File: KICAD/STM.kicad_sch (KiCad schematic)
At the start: 1 part, among them IC5 STM32F746BGT6

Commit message: BT + PCM1808
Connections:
- net SAI1_MCLK_A/SCKI: now reaches IC5.1 (PE2)
- net USART_TX: now reaches IC5.143 (PA9)
- net USART_RX: now reaches IC5.144 (PA10)
- net SAI1_FS_A/LRCK: now reaches IC5.3 (PE4)
- net SAI1_SCK_A/BCK: now reaches IC5.4 (PE5)
- net JACK_DET: now reaches IC5.45 (PA2)
- net SAI1_SD_A/DOUT: now reaches IC5.5 (PE6)
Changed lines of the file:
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@@
 	(generator_version "9.0")
 	(paper "A3")
+	(wire
+		(pts
+			(xy 120.65 81.28) (xy 135.89 81.28)
+		)
+		(stroke
+			(width 0)
+			(type default)
+		)
+	)
+	(wire
+		(pts
+			(xy 280.67 101.6) (xy 292.1 101.6)
+		)
+		(stroke
+			(width 0)
+			(type default)
+		)
+	)
+	(wire
+		(pts
+			(xy 280.67 104.14) (xy 292.1 104.14)
+		)
+		(stroke
+			(width 0)
+			(type default)
+		)
+	)
+	(wire
+		(pts
+			(xy 120.65 78.74) (xy 135.89 78.74)
+		)
+		(stroke
+			(width 0)
+			(type default)
+		)
+	)
+	(wire
+		(pts
+			(xy 120.65 71.12) (xy 135.89 71.12)
+		)
+		(stroke
+			(width 0)
+			(type default)
+		)
+	)
+	(wire
+		(pts
+			(xy 120.65 76.2) (xy 135.89 76.2)
+		)
+		(stroke
+			(width 0)
+			(type default)
+		)
+	)
+	(hierarchical_label "USART_TX"
+		(shape input)
+		(at 292.1 104.14 0)
+		(effects
+			(font
+				(size 1.27 1.27)
+			)
+			(justify left)
+		)
+	)
+	(hierarchical_label "SAI1_FS_A{slash}LRCK"
+		(shape input)
+		(at 120.65 76.2 180)
+		(effects
+			(font
+				(size 1.27 1.27)
+			)
+			(justify right)
+		)
+	)
+	(hierarchical_label "SAI1_SCK_A{slash}BCK"
+		(shape input)
+		(at 120.65 78.74 180)
+		(effects
+			(font
+				(size 1.27 1.27)
+			)
+			(justify right)
+		)
+	)
+	(hierarchical_label "SAI1_MCLK_A{slash}SCKI"
+		(shape input)
+		(at 120.65 71.12 180)
+		(effects
+			(font
+				(size 1.27 1.27)
+			)
+			(justify right)
+		)
+	)
+	(hierarchical_label "USART_RX"
+		(shape input)
+		(at 292.1 101.6 0)
+		(effects
+			(font
+				(size 1.27 1.27)
+			)
+			(justify left)
+		)
+	)
+	(hierarchical_label "SAI1_SD_A{slash}DOUT"
+		(shape input)
+		(at 120.65 81.28 180)
+		(effects
+			(font
+				(size 1.27 1.27)
+			)
+			(justify right)
+		)
+	)
+	(hierarchical_label "JACK_DET"
+		(shape input)
+		(at 135.89 182.88 180)
+		(effects
+			(font
+				(size 1.27 1.27)
+			)
+			(justify right)
+		)
+	)
 	(symbol
 		(lib_id "STM32F746BGT6:STM32F746BGT6")

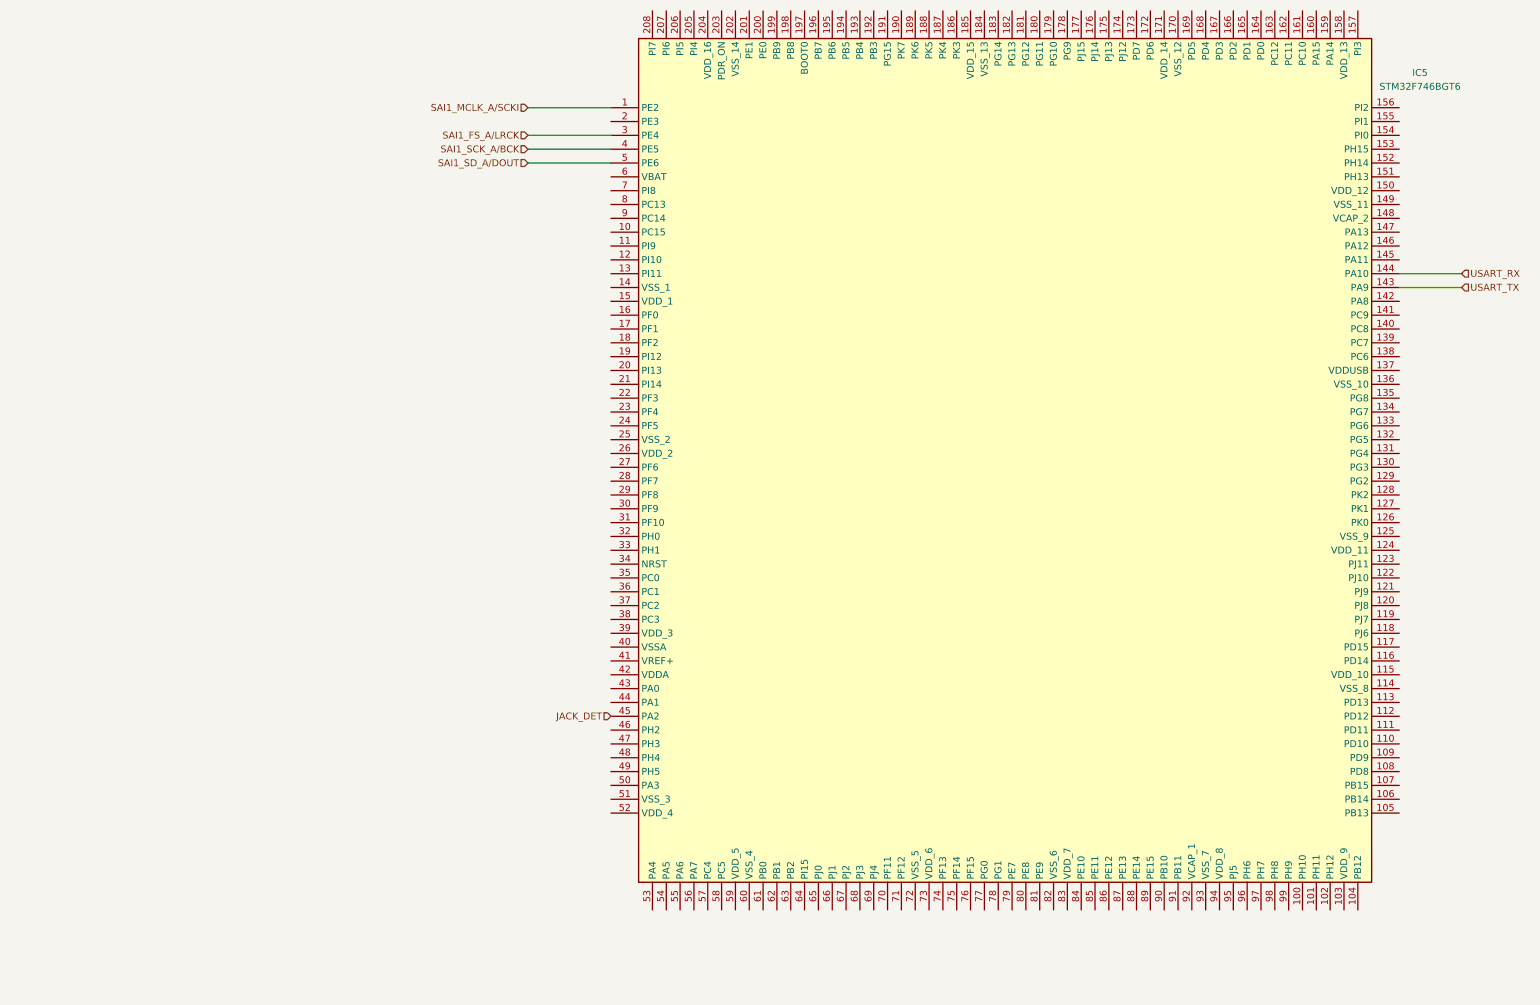
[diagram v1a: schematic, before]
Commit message: Config ports DAC + Ampli
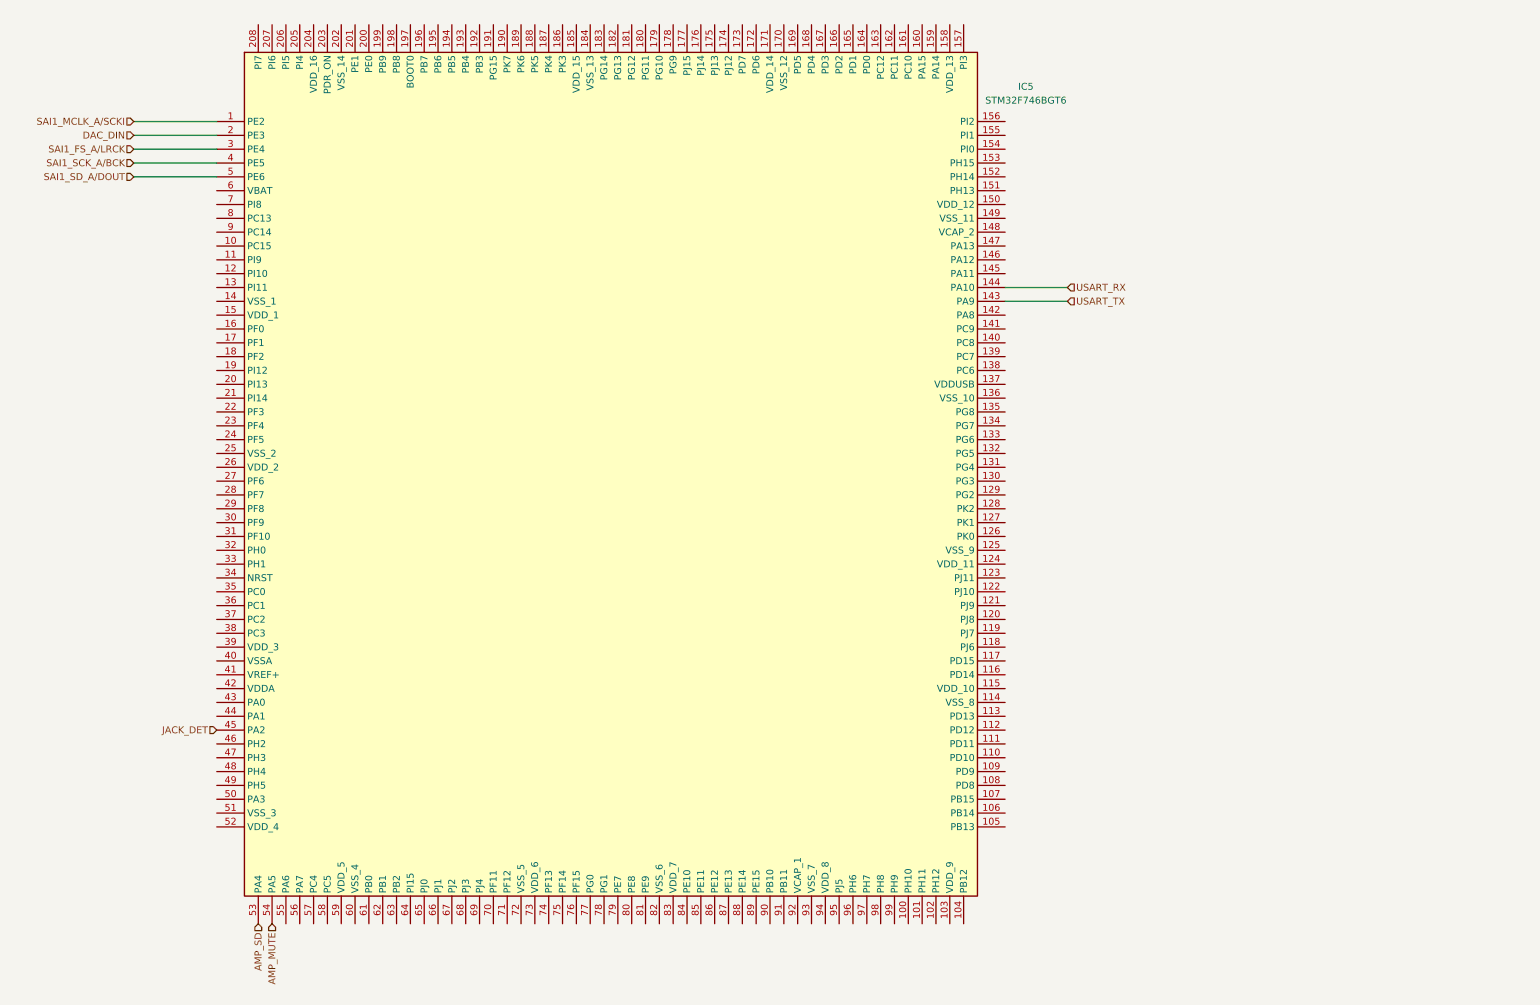
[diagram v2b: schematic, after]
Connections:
- net DAC_DIN: now reaches IC5.2 (PE3)
- net AMP_SD: now reaches IC5.53 (PA4)
- net AMP_MUTE: now reaches IC5.54 (PA5)
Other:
- moved on the sheet: IC5
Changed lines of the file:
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@@
 	(wire
 		(pts
-			(xy 120.65 81.28) (xy 135.89 81.28)
-		)
-		(stroke
-			(width 0)
-			(type default)
-		)
-	)
-	(wire
-		(pts
-			(xy 280.67 101.6) (xy 292.1 101.6)
-		)
-		(stroke
-			(width 0)
-			(type default)
-		)
-	)
-	(wire
-		(pts
-			(xy 280.67 104.14) (xy 292.1 104.14)
-		)
-		(stroke
-			(width 0)
-			(type default)
-		)
-	)
-	(wire
-		(pts
-			(xy 120.65 78.74) (xy 135.89 78.74)
-		)
-		(stroke
-			(width 0)
-			(type default)
-		)
-	)
-	(wire
-		(pts
-			(xy 120.65 71.12) (xy 135.89 71.12)
-		)
-		(stroke
-			(width 0)
-			(type default)
-		)
-	)
-	(wire
-		(pts
-			(xy 120.65 76.2) (xy 135.89 76.2)
+			(xy 48.26 76.2) (xy 63.5 76.2)
+		)
+		(stroke
+			(width 0)
+			(type default)
+		)
+	)
+	(wire
+		(pts
+			(xy 48.26 83.82) (xy 63.5 83.82)
+		)
+		(stroke
+			(width 0)
+			(type default)
+		)
+	)
+	(wire
+		(pts
+			(xy 208.28 104.14) (xy 219.71 104.14)
+		)
+		(stroke
+			(width 0)
+			(type default)
+		)
+	)
+	(wire
+		(pts
+			(xy 208.28 106.68) (xy 219.71 106.68)
+		)
+		(stroke
+			(width 0)
+			(type default)
+		)
+	)
+	(wire
+		(pts
+			(xy 48.26 81.28) (xy 63.5 81.28)
+		)
+		(stroke
+			(width 0)
+			(type default)
+		)
+	)
+	(wire
+		(pts
+			(xy 48.26 73.66) (xy 63.5 73.66)
+		)
+		(stroke
+			(width 0)
+			(type default)
+		)
+	)
+	(wire
+		(pts
+			(xy 48.26 78.74) (xy 63.5 78.74)
 		)
 		(stroke
@@
 	(hierarchical_label "USART_TX"
 		(shape input)
-		(at 292.1 104.14 0)
+		(at 219.71 106.68 0)
 		(effects
 			(font
@@
 	(hierarchical_label "SAI1_FS_A{slash}LRCK"
 		(shape input)
-		(at 120.65 76.2 180)
+		(at 48.26 78.74 180)
 		(effects
 			(font
@@
 	(hierarchical_label "SAI1_SCK_A{slash}BCK"
 		(shape input)
-		(at 120.65 78.74 180)
+		(at 48.26 81.28 180)
 		(effects
 			(font
@@
 	(hierarchical_label "SAI1_MCLK_A{slash}SCKI"
 		(shape input)
-		(at 120.65 71.12 180)
+		(at 48.26 73.66 180)
 		(effects
 			(font
@@
 	(hierarchical_label "USART_RX"
 		(shape input)
-		(at 292.1 101.6 0)
+		(at 219.71 104.14 0)
 		(effects
 			(font
@@
 		)
 	)
+	(hierarchical_label "DAC_DIN"
+		(shape input)
+		(at 48.26 76.2 180)
+		(effects
+			(font
+				(size 1.27 1.27)
+			)
+			(justify right)
+		)
+	)
 	(hierarchical_label "SAI1_SD_A{slash}DOUT"
 		(shape input)
-		(at 120.65 81.28 180)
+		(at 48.26 83.82 180)
+		(effects
+			(font
+				(size 1.27 1.27)
+			)
+			(justify right)
+		)
+	)
+	(hierarchical_label "AMP_SD"
+		(shape input)
+		(at 71.12 220.98 270)
+		(effects
+			(font
+				(size 1.27 1.27)
+			)
+			(justify right)
+		)
+	)
+	(hierarchical_label "AMP_MUTE"
+		(shape input)
+		(at 73.66 220.98 270)
 		(effects
 			(font
@@
 	(hierarchical_label "JACK_DET"
 		(shape input)
-		(at 135.89 182.88 180)
+		(at 63.5 185.42 180)
 		(effects
 			(font
@@
 	(symbol
 		(lib_id "STM32F746BGT6:STM32F746BGT6")
-		(at 135.89 71.12 0)
+		(at 63.5 73.66 0)
 		(unit 1)
 		(exclude_from_sim no)
@@
 		(fields_autoplaced yes)
 		(property "Reference" "IC5"
-			(at 284.48 64.6998 0)
+			(at 212.09 67.2398 0)
 			(effects
 				(font
@@
 		)
 		(property "Value" "STM32F746BGT6"
-			(at 284.48 67.2398 0)
+			(at 212.09 69.7798 0)
 			(effects
 				(font
@@
 		)
 		(property "Footprint" "STM32F746BGT6:QFP50P3000X3000X160-208N"
-			(at 276.86 155.88 0)
+			(at 204.47 158.42 0)
 			(effects
 				(font
@@
 		)
 		(property "Datasheet" "https://www.st.com/resource/en/datasheet/stm32f745ie.pdf"
-			(at 276.86 255.88 0)
+			(at 204.47 258.42 0)
 			(effects
 				(font
@@
 		)
 		(property "Description" "ARM-based Cortex-M7 32b MCU+FPU, 462DMIPS, up to 1MB Flash/320+16+ 4KB RAM, USB OTG HS/FS, ethernet, 18 TIMs, 3 ADCs, 25 com itf, cam & LCD"
-			(at 135.89 71.12 0)
+			(at 63.5 73.66 0)
 			(effects
 				(font
@@
 		)
 		(property "Height" "1.6"
-			(at 276.86 455.88 0)
+			(at 204.47 458.42 0)
 			(effects
 				(font
@@
 		)
 		(property "Manufacturer_Name" "STMicroelectronics"
-			(at 276.86 555.88 0)
+			(at 204.47 558.42 0)
 			(effects
 				(font
@@
 		)
 		(property "Manufacturer_Part_Number" "STM32F746BGT6"
-			(at 276.86 655.88 0)
+			(at 204.47 658.42 0)
 			(effects
 				(font
@@
 		)
 		(property "Mouser Part Number" "511-STM32F746BGT6"
-			(at 276.86 755.88 0)
+			(at 204.47 758.42 0)
 			(effects
 				(font
@@
 		)
 		(property "Mouser Price/Stock" "https://www.mouser.co.uk/ProductDetail/STMicroelectronics/STM32F746BGT6?qs=E2FFEhwHWtcSD54rSf3kgw%3D%3D"
-			(at 276.86 855.88 0)
+			(at 204.47 858.42 0)
 			(effects
 				(font
@@
 		)
 		(property "Arrow Part Number" "STM32F746BGT6"
-			(at 276.86 955.88 0)
+			(at 204.47 958.42 0)
 			(effects
 				(font
@@
 		)
 		(property "Arrow Price/Stock" "https://www.arrow.com/en/products/stm32f746bgt6/stmicroelectronics?utm_currency=USD&region=nac"
-			(at 276.86 1055.88 0)
-			(effects
-				(font
+			(at 204.47 1058.42 0)
+			(effects
+				(font
